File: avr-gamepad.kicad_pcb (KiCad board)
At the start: 2 copper layers, 28.2 x 83.9 mm, 33 parts, among them J1 Conn_01x08, J2 Conn_01x08, P1 USB_C_Plug_USB2.0, SW10 Up, SW11 Down, SW12 Left, SW13 Select, SW2 R, SW3 X, SW4 A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

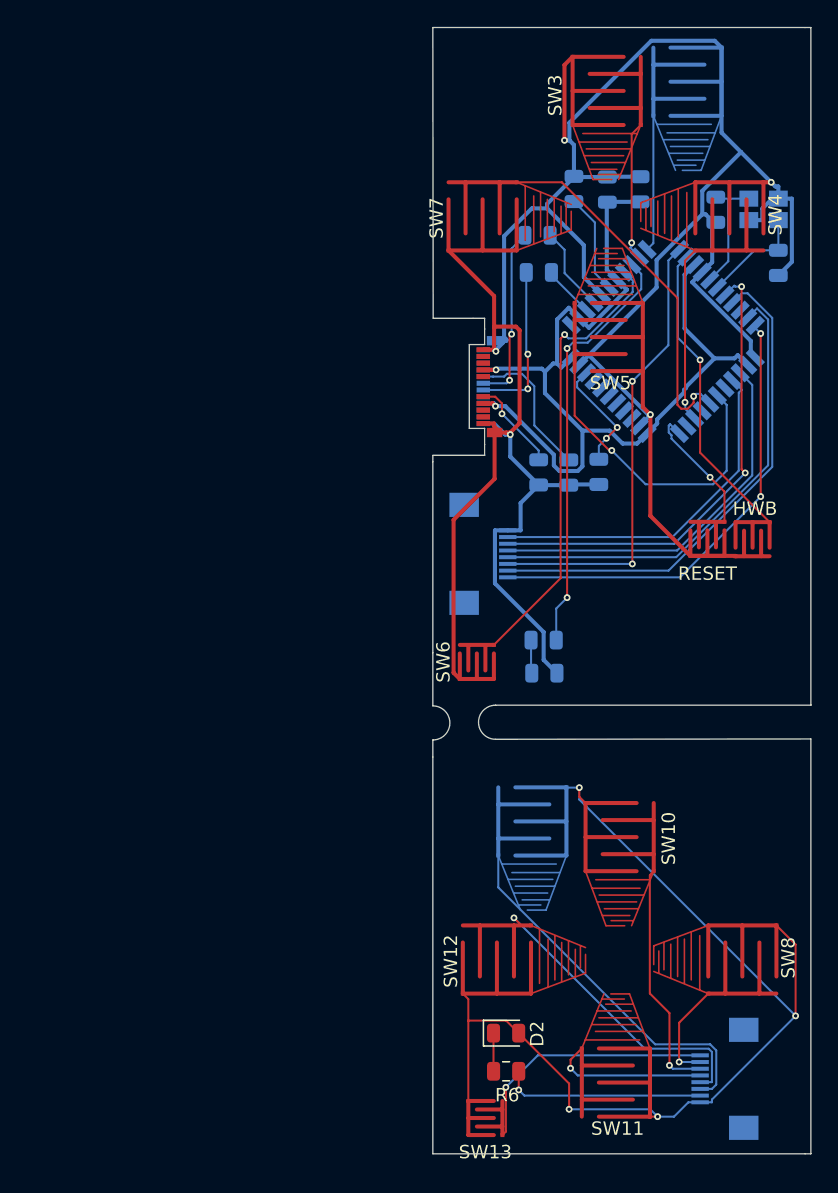
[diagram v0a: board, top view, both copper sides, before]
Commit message: add 0.1 in headers, label atmega pins better
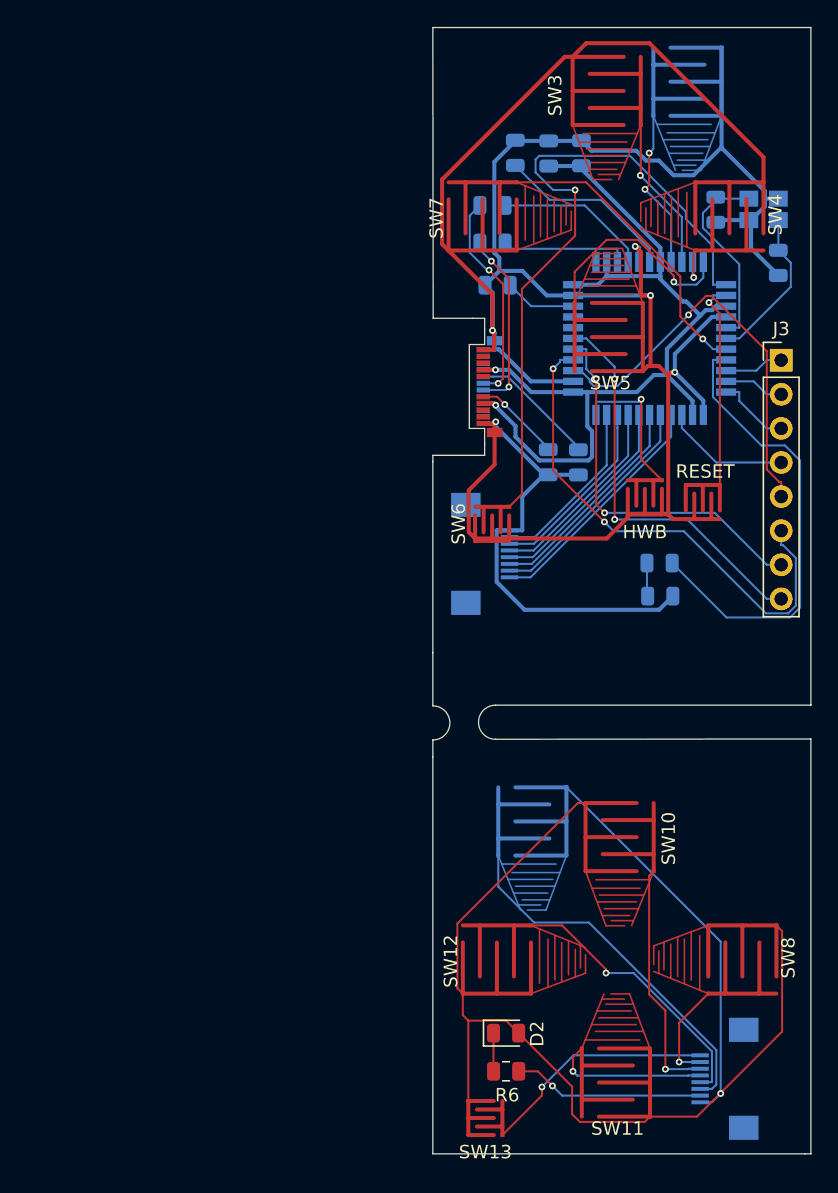
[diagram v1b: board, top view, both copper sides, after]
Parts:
- removed the HWB at (151.3, 118.5)
- added J3: Conn_01x08_Female, Connector_PinHeader_2.54mm:PinHeader_1x08_P2.54mm_Vertical, F.Cu at (153.4, 105.2)
- added RESET: RESET, button-contacts:Small, F.Cu at (147.6, 115.8)
- HWB: renamed from RESET; value SW_Push -> HWB
- moved C5 15.8 mm to (132.3, 99.6), turned to 180 degrees
- moved R5 10.4 mm to (144.3, 120.3)
- moved D1 10.4 mm to (144.4, 122.8)
- moved SW6 10.4 mm to (131.9, 117.4)
- moved HWB 5.60 mm to (143.3, 115.4)
- moved C1 5.13 mm to (136.1, 89.8)
- moved C2 5.13 mm to (138.5, 89.8)
- moved C6 5.13 mm to (133.6, 89.8)
- moved R2 4.09 mm to (131.9, 96.5)
- moved R1 4.02 mm to (131.9, 93.7)
- moved R3 1.04 mm to (136.1, 112.8)
- moved R4 1.04 mm to (138.3, 112.8)
- moved U1 1.04 mm to (143.6, 103.6), turned to 270 degrees
- moved J2 0.13 mm to (131.3, 119.6)
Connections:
- net Net-(U1-Pad1) renamed /pe6-1
- net Net-(U1-Pad40) renamed /pf1-40
- net Net-(U1-Pad41) renamed /pf0-41
- J2 pad 1: /pd5 -> /pd6-26
- J2 pad 2: /pd1 -> /pd7-27
- J2 pad 3: /pb7 -> /pb4-28
- J2 pad 4: /pd3 -> /pb5-29
- J2 pad 5: /pd4 -> /pb6-30
- J2 pad 6: /pd0 -> /pc6-31
- J2 pad 7: /pd6 -> /pc7-32
- R5 pad 2: /pb1 -> /pd1-19
- SW2 pad 1: /pb3 -> /pb0-8
- SW3 pad 1: /pb2 -> /pb1-9
- SW4 pad 1: /pc6 -> /pb2-10
- SW5 pad 1: /pb4 -> /pb3-11
- SW6 pad 1: /pb0 -> /pb7-12
- SW7 pad 1: /pb5 -> /pd0-18
- U1 pad 10: /pb2 -> /pb2-10
- U1 pad 11: /pb3 -> /pb3-11
- U1 pad 12: /pb7 -> /pb7-12
- U1 pad 18: /pd0 -> /pd0-18
- U1 pad 19: /pd1 -> /pd1-19
- U1 pad 20: /pd2 -> /pd2-20
- U1 pad 21: /pd3 -> /pd3-21
- U1 pad 22: /pd5 -> /pd5-22
- U1 pad 25: /pd4 -> /pd4-25
- U1 pad 26: /pd6 -> /pd6-26
- U1 pad 27: /pd7 -> /pd7-27
- U1 pad 28: /pb4 -> /pb4-28
- U1 pad 29: /pb5 -> /pb5-29
- U1 pad 30: /pb6 -> /pb6-30
- U1 pad 31: /pc6 -> /pc6-31
- U1 pad 32: /pc7 -> /pc7-32
- U1 pad 36: Net-(U1-Pad36) -> /pf7-36
- U1 pad 37: Net-(U1-Pad37) -> /pf6-37
- U1 pad 38: Net-(U1-Pad38) -> /pf5-38
- U1 pad 39: Net-(U1-Pad39) -> /pf4-39
- U1 pad 8: /pb0 -> /pb0-8
- U1 pad 9: /pb1 -> /pb1-9
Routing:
- net /pb7-12: track 0.00 -> 50.4 mm, vias 0 -> 1
- net /pf6-37: track 0.00 -> 38.3 mm, vias 0 -> 2
- net /pd1: track 38.0 -> 0.00 mm
- net /pd0: track 35.4 -> 0.00 mm, vias 2 -> 0
- net /pd3: track 35.2 -> 0.00 mm
- net /pd1-19: track 0.00 -> 34.7 mm
- net /pd5: track 34.3 -> 0.00 mm, vias 2 -> 0
- net /pb7: track 34.2 -> 0.00 mm, vias 2 -> 0
- net /pb0: track 33.7 -> 0.00 mm, vias 1 -> 0
- net /pb1: track 31.5 -> 0.00 mm, vias 2 -> 0
- net /pf7-36: track 0.00 -> 30.9 mm, vias 0 -> 1
- net /pf4-39: track 0.00 -> 30.2 mm, vias 0 -> 2
- net /pd4: track 28.6 -> 0.00 mm
- net /pf5-38: track 0.00 -> 28.5 mm, vias 0 -> 2
- net /pb4: track 28.2 -> 0.00 mm, vias 1 -> 0
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
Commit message: move board outline for each half
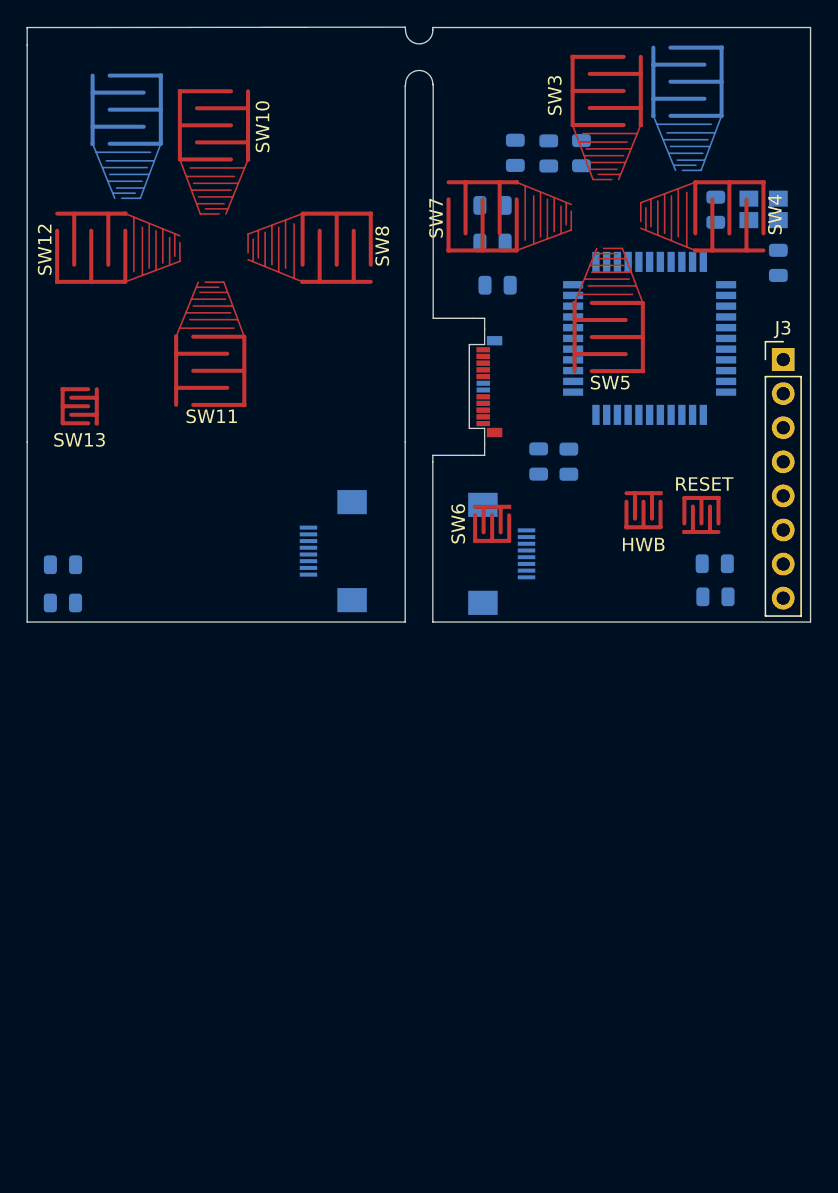
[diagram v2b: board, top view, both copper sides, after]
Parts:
- D2, R6: moved to B.Cu
- moved SW10 61.0 mm to (111.2, 87.7)
- moved SW12 61.0 mm to (102.0, 96.8)
- moved SW8 61.0 mm to (120.3, 96.8)
- moved SW9 61.0 mm to (104.6, 86.5)
- moved SW11 61.0 mm to (110.9, 106.0)
- moved SW13 61.0 mm to (101.1, 108.6)
- moved R6 50.1 mm to (99.9, 120.4)
- moved J1 49.0 mm to (120.0, 119.4)
- moved D2 46.0 mm to (99.9, 123.3)
- moved D1 4.12 mm to (148.5, 122.8)
- moved R5 4.12 mm to (148.5, 120.4)
- moved J2 1.27 mm to (132.6, 119.6)
- moved RESET 0.97 mm to (147.5, 116.7)
- moved HWB 0.97 mm to (143.2, 116.4)
- moved R3 0.71 mm to (135.3, 112.8)
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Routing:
- net GND: track 222.2 -> 0.00 mm, vias 5 -> 0
- net Net-(D2-Pad2): track 94.8 -> 0.00 mm, vias 1 -> 0
- net +5V: track 69.0 -> 0.00 mm, vias 2 -> 0
- net /pb7-12: track 50.4 -> 0.00 mm, vias 1 -> 0
- net /pf6-37: track 38.3 -> 0.00 mm, vias 2 -> 0
- net /pd1-19: track 34.7 -> 0.00 mm
- net /pf7-36: track 30.9 -> 0.00 mm, vias 1 -> 0
- net /pf4-39: track 30.2 -> 0.00 mm, vias 2 -> 0
- net /pf5-38: track 28.5 -> 0.00 mm, vias 2 -> 0
- net Net-(J1-Pad6): track 27.5 -> 0.00 mm
- net /pd0-18: track 22.5 -> 0.00 mm, vias 1 -> 0
- net Net-(J1-Pad5): track 20.7 -> 0.00 mm, vias 1 -> 0
- net /pd6-26: track 18.0 -> 0.00 mm
- net Net-(J1-Pad3): track 18.0 -> 0.00 mm, vias 1 -> 0
- net Net-(J1-Pad1): track 17.6 -> 0.00 mm, vias 1 -> 0
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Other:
- board size 28.2 x 83.9 mm -> 58.4 x 44.3 mm

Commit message: route, more mousebites
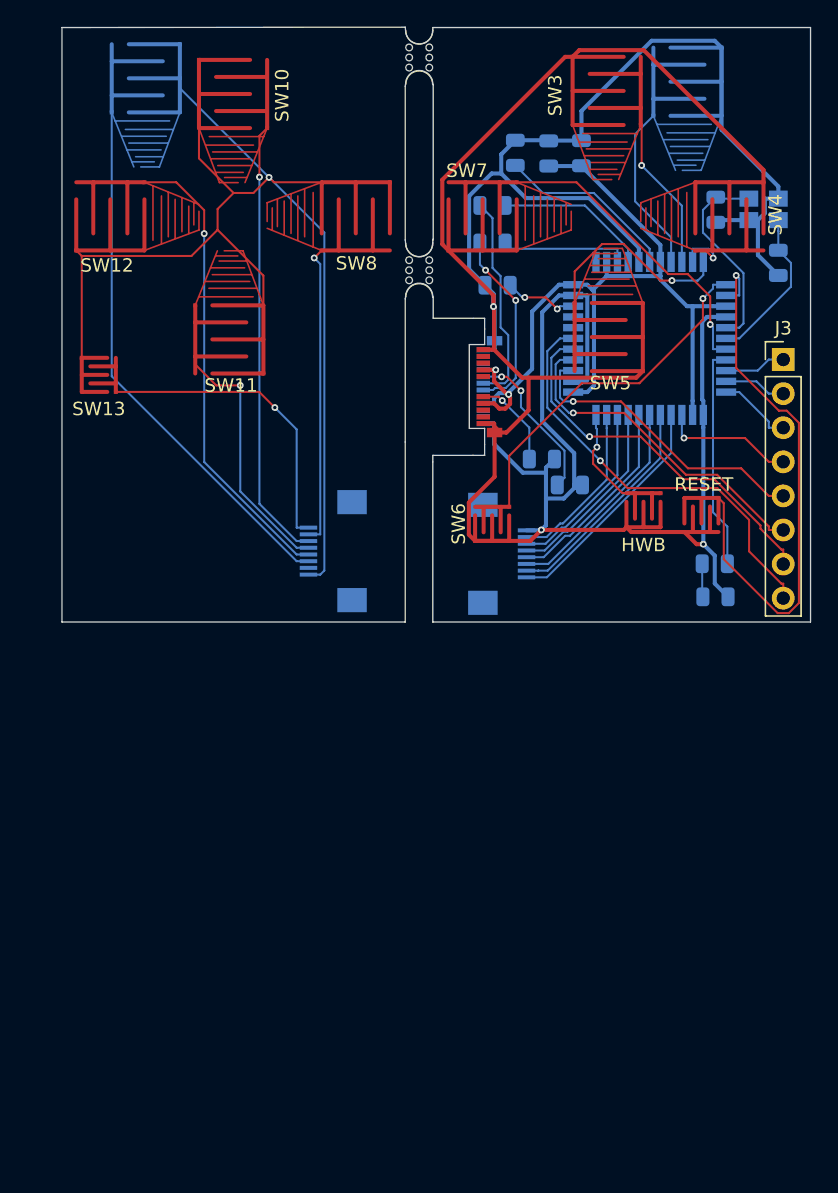
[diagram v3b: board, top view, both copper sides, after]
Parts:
- removed D2: LED, LED_SMD:LED_0805_2012Metric
- removed R6: 1K, Resistor_SMD:R_0805_2012Metric
- added mouse-bite-2mm-slot: VAL**, Panelization:mouse-bite-2mm-slot, F.Cu at (126.4, 98.5)
- added mouse-bite-2mm-slot: VAL**, Panelization:mouse-bite-2mm-slot, F.Cu at (126.4, 82.7)
- moved SW11 2.74 mm to (112.3, 103.7)
- moved SW13 2.74 mm to (102.6, 106.3)
- moved SW9 2.74 mm to (106.1, 84.2)
- moved SW10 2.74 mm to (112.6, 85.4)
- moved SW12 2.74 mm to (103.4, 94.5)
- moved SW8 2.74 mm to (121.7, 94.5)
- moved R4 1.74 mm to (137.7, 114.5), turned to 0 degrees
- moved R3 0.30 mm to (135.6, 112.6), turned to 0 degrees
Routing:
- net GND: track 0.00 -> 236.0 mm, vias 0 -> 3
- net Net-(D2-Pad2): track 0.00 -> 102.7 mm, vias 0 -> 1
- net +5V: track 0.00 -> 64.8 mm, vias 0 -> 2
- net Net-(SW1-Pad2): track 0.00 -> 41.6 mm, vias 0 -> 1
- net Net-(J1-Pad6): track 0.00 -> 40.0 mm
- net Net-(J1-Pad5): track 0.00 -> 34.7 mm, vias 0 -> 1
- net Net-(J1-Pad3): track 0.00 -> 33.0 mm, vias 0 -> 1
- net /pf4-39: track 0.00 -> 32.0 mm, vias 0 -> 1
- net /pf5-38: track 0.00 -> 28.2 mm, vias 0 -> 1
- net /pb7-12: track 0.00 -> 26.3 mm, vias 0 -> 1
- net /pf6-37: track 0.00 -> 25.2 mm, vias 0 -> 1
- net Net-(J1-Pad4): track 0.00 -> 23.1 mm, vias 0 -> 1
- net /pd0-18: track 0.00 -> 22.9 mm, vias 0 -> 1
- net Net-(J1-Pad1): track 0.00 -> 22.8 mm, vias 0 -> 1
- net /pf7-36: track 0.00 -> 22.7 mm, vias 0 -> 1
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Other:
- board size 58.4 x 44.3 mm -> 55.8 x 44.3 mm

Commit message: silkscreen credits and art
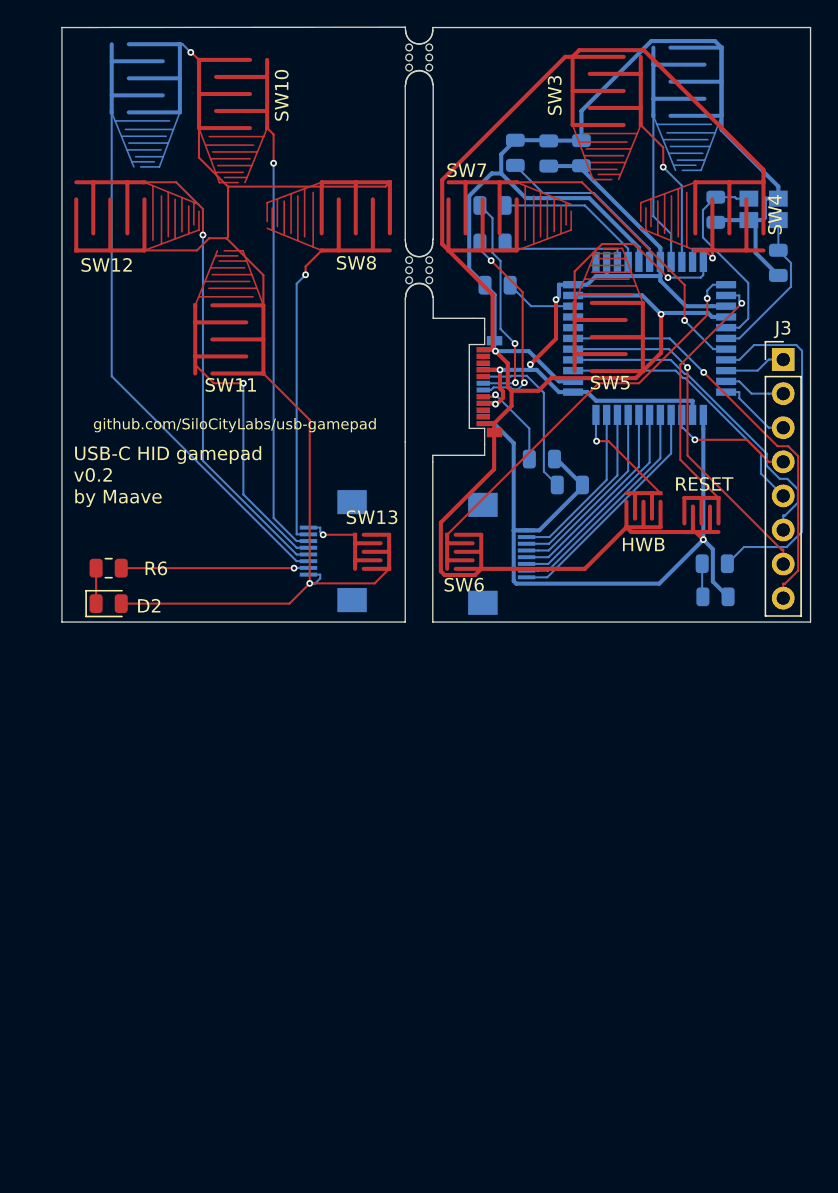
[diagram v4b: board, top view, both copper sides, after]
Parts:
- added D2: LED, LED_SMD:LED_0805_2012Metric, F.Cu at (103.3, 123.3)
- added G***: LOGO, drawing:F.Silk_g32, B.Cu at (112.7, 106.0)
- added G***: LOGO, squidward:loser_silkscreen, B.Cu at (143.2, 103.5)
- added R6: 1K, Resistor_SMD:R_0805_2012Metric, F.Cu at (103.3, 120.7)
- C3, C4: value 10pF -> 22pF
- mb-2mm-1: renamed from mouse-bite-2mm-slot; value VAL** -> mb1
- mb-2mm-2: renamed from mouse-bite-2mm-slot; value VAL** -> mb2
- moved SW13 24.3 mm to (122.9, 119.5), turned to 180 degrees
- moved SW6 2.95 mm to (129.8, 119.5), turned to 180 degrees
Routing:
- net Net-(SW1-Pad2): track 41.6 -> 19.2 mm
- net Net-(J1-Pad1): track 22.8 -> 3.88 mm
- net GND: track 236.0 -> 252.6 mm
- net Net-(J1-Pad7): track 0.00 -> 14.0 mm, vias 0 -> 1
- net Net-(D2-Pad2): track 102.7 -> 91.3 mm, vias 1 -> 2
- net /pd1-19: track 16.6 -> 26.3 mm
- net +5V: track 64.8 -> 58.9 mm, vias 2 -> 4
- net /pb7-12: track 26.3 -> 29.6 mm
- net Net-(D2-Pad1): track 0.00 -> 2.64 mm
- net /pf7-36: track 22.7 -> 20.4 mm, vias 1 -> 0
- net /pf5-38: track 28.2 -> 26.8 mm
- net Net-(SW14-Pad1): track 9.72 -> 8.35 mm
- net Net-(P1-PadA7): track 14.0 -> 15.2 mm
- net /pb0-8: track 12.6 -> 11.4 mm
- net Net-(P1-PadA6): track 15.8 -> 16.7 mm, vias 0 -> 2
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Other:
- board text added: "USB-C HID gamepad v0.2 by Maave"
- board text added: "github.com/SiloCityLabs/usb-gamepad"

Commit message: no art. Checkpoint before analog
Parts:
- removed the G*** at (112.7, 106.0)
